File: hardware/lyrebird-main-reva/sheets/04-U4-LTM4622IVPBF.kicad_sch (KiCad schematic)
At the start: 13 parts, among them U4 LTM4622IV#PBF

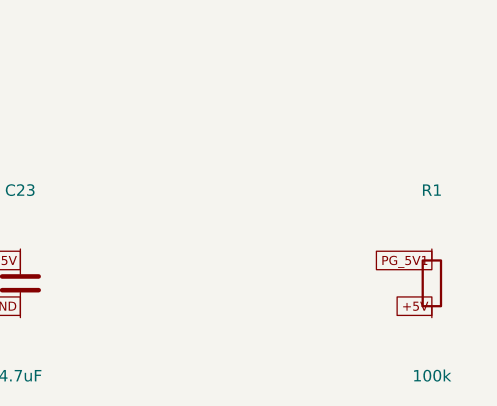
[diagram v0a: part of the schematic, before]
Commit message: Connect two power-good nets that were connected to nothing
The schematic validator found a confirmed fault, and it is the kind that
reads as correct code. `Net("PG_5V")` appears twice in main_board.py --
once to attach the buck's power-good pin, once to attach its pull-up --
and SKiDL creates a NEW net on each call, uniquifying the second name.
The result was four single-node nets: both LMR33630 power-good pins
alone, and both 100 k resistors with one lead floating.

The inverter's half mattered more than the buck's. U7's GND pin *is*
-6V_A, so 100 k to system ground is a pull-up relative to the device and
the only way that flag can be read at all. It was reading nothing.

Both now use one Net object and reuse it, which is what every other net
in both generators already did -- the defect was exactly two instances of
one idiom, not a pattern. I checked: MCLK is also written as
Net("MCLK") twice, but once per file on different boards, so it is
whole in each netlist.

The more useful outcome is a check. A net with one node connects
nothing, and nothing in the generation path said so -- KiCad ERC would
have, on import, and nothing runs ERC. check_freshness.py now reports
single-node nets on both boards, with the module's four reserved element
lines exempted because interface.md requires the main board to drive
them and they are correctly bare on the module side. Tamper-tested by
reintroducing the idiom: it names PG_5V and PG_5V1 and fails.

Co-Authored-By: Claude Opus 5 <noreply@anthropic.com>
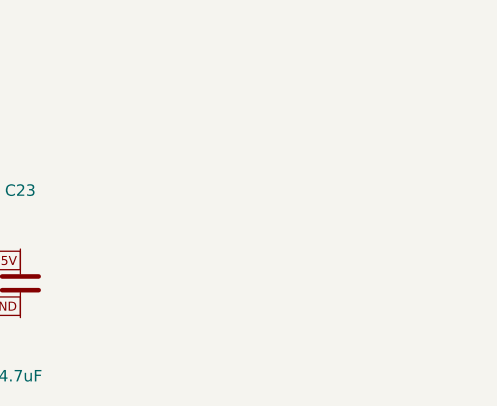
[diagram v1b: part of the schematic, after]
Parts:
- removed R1: 100k, symbol Device:R
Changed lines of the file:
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@@
 		(instances (project "" (path "/" (reference "C23") (unit 1))))
-	)
-	(symbol (lib_id "Device:R") (at 167.64000000000001 175.26 0) (unit 1)
-		(exclude_from_sim no) (in_bom yes) (on_board yes) (dnp no)
-		(property "Reference" "R1" (at 167.64000000000001 164.95 0)
-			(effects (font (size 1.27 1.27))))
-		(property "Value" "100k" (at 167.64000000000001 185.57 0)
-			(effects (font (size 1.27 1.27))))
-		(instances (project "" (path "/" (reference "R1") (unit 1))))
 	)
 	(wire (pts (xy 124.46000000000001 66.04) (xy 124.46000000000001 109.22))
@@
 )
 	(global_label "+5V" (shape passive) (at 121.92 172.72 0)
-		(effects (font (size 1.0 1.0)) (justify right))
-)
-	(global_label "+5V" (shape passive) (at 167.64000000000001 177.8 0)
 		(effects (font (size 1.0 1.0)) (justify right))
 )
@@
 		(effects (font (size 1.0 1.0)) (justify right))
 )
-	(global_label "PG_5V1" (shape passive) (at 167.64000000000001 172.72 0)
-		(effects (font (size 1.0 1.0)) (justify right))
-)

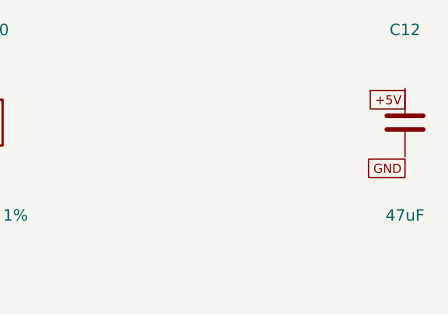
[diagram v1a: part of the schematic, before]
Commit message: Act on the schematic validation: three faults and the core-rail guard
**The SuperSpeed pairs were wired backwards, and are now not wired.**
USB_SSRX_P/N were the only multi-node nets on the board with an INPUT at
every pin -- the receptacle's SSRX pins are inputs and so are the
bridge's RIDP/RIDN, so nothing drove them, and the transmit pair was
mirrored the same way. The comment asserted a crossover inside the cable
as fact and reasoned from it; USB 3.0 cables have no crossover.
SuperSpeed would never have trained and the link would have fallen back
to 480 Mb/s silently -- which is the speed 0014 chose on purpose, since
no galvanic isolator exists above USB 2.0. So the pairs are removed
rather than corrected, which also retires the hardest constraint in this
board's layout. How to wire them correctly if they ever come back is
recorded where they were.

**The inverting converter had no input capacitor across its own
terminals.** Nothing spanned +12V and -6V_A, and U7's GND pin *is*
-6V_A, so the loop its switching current actually takes was unbypassed
-- the input caps near U5 are referenced to system ground and are not in
that loop at all. This is the third fault found in U7 and all three are
the same mistake: reasoning about it as though its ground were the
board's.

**The translator's output enables are tied low against an explicit
datasheet instruction**, and the fix is sequencing rather than a pull-up.
SCES576I says OE must be pulled up to VCCA and not enabled until both
supplies are stable; a pull-up is not available here because nothing on
the module could pull it down -- no spare mezzanine pin, and MUTE_N has
the wrong polarity. Instead VCC(A) is made the last rail to arrive:
10 uF on U9's SET gives 573 ms against 359 ms for VCC(B), so the enable
cannot precede the supply it switches to. It costs nothing, because that
rail feeds the translator's reference supply and nothing else.

**The core rail now has a guard, and it needed two attempts.** The
existing as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
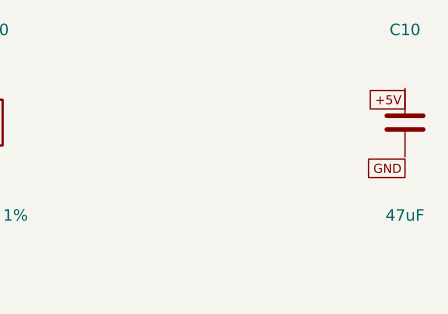
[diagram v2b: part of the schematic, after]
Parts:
- renumbered C12 to C10
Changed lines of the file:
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@@
 	(symbol (lib_id "Device:C") (at 170.18 35.56 0) (unit 1)
 		(exclude_from_sim no) (in_bom yes) (on_board yes) (dnp no)
-		(property "Reference" "C12" (at 170.18 25.250000000000004 0)
+		(property "Reference" "C10" (at 170.18 25.250000000000004 0)
 			(effects (font (size 1.27 1.27))))
 		(property "Value" "47uF" (at 170.18 45.870000000000005 0)
 			(effects (font (size 1.27 1.27))))
-		(instances (project "" (path "/" (reference "C12") (unit 1))))
+		(instances (project "" (path "/" (reference "C10") (unit 1))))
 	)
 	(symbol (lib_id "Device:C") (at 35.56 175.26 0) (unit 1)
@@
 		(instances (project "" (path "/" (reference "C23") (unit 1))))
 	)
-	(wire (pts (xy 124.46000000000001 66.04) (xy 124.46000000000001 109.22))
-		(stroke (width 0) (type default)))
-	(wire (pts (xy 124.46000000000001 109.22) (xy 96.52 109.22))
-		(stroke (width 0) (type default)))
-	(wire (pts (xy 35.56 111.76) (xy 96.52 111.76))
-		(stroke (width 0) (type default)))
 	(wire (pts (xy 124.46000000000001 33.02) (xy 124.46000000000001 116.84))
 		(stroke (width 0) (type default)))
@@
 	(wire (pts (xy 81.28 116.84) (xy 96.52 116.84))
 		(stroke (width 0) (type default)))
+	(wire (pts (xy 124.46000000000001 66.04) (xy 124.46000000000001 109.22))
+		(stroke (width 0) (type default)))
+	(wire (pts (xy 124.46000000000001 109.22) (xy 96.52 109.22))
+		(stroke (width 0) (type default)))
+	(wire (pts (xy 35.56 111.76) (xy 96.52 111.76))
+		(stroke (width 0) (type default)))
 	(wire (pts (xy 35.56 66.04) (xy 35.56 119.38))
